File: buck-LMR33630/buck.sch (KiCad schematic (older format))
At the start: 22 parts, among them J1 USB-C Connector, P1 BATT-P, P2 BATT-N, P3 5V, SW1 RST, U1 LMR33630ADDA

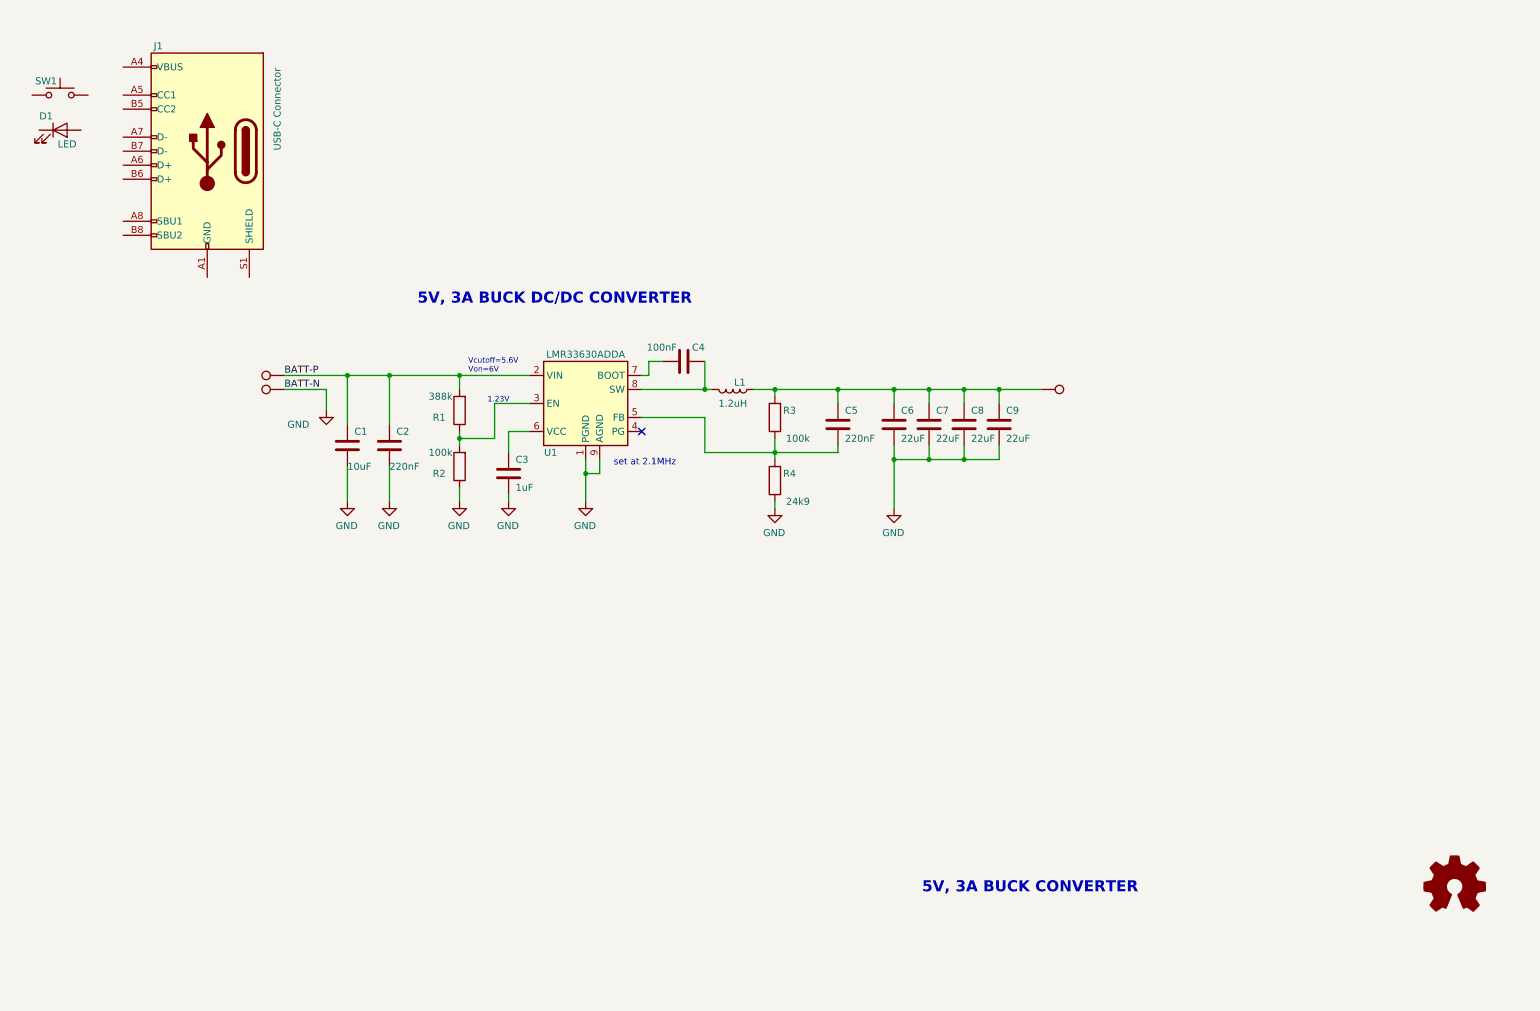
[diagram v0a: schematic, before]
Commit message: routed buck converter and added usb type c connector
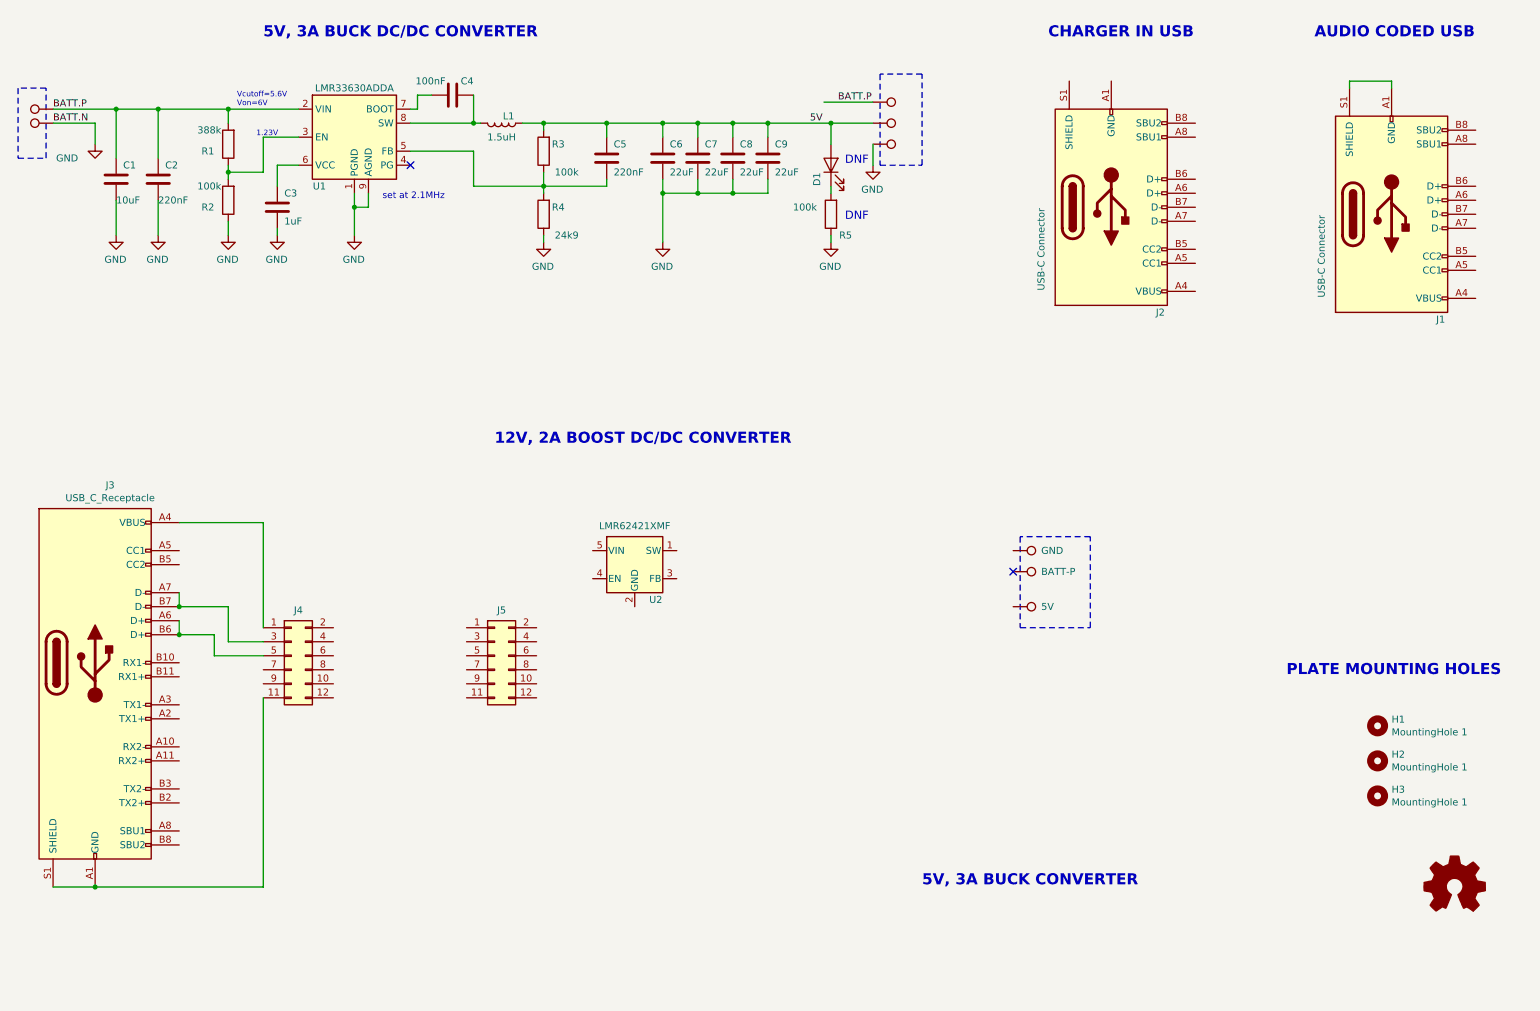
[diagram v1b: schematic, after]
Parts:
- removed SW1: RST, Button_Switch_SMD:SW_SPST_FSMSM, symbol Switch:SW_Push
- added H1, H2, H3: MountingHole 1, MountingHole:MountingHole_3.2mm_M3_Pad_Via, symbol Mechanical:MountingHole
- added J2: USB-C Connector, Connector_USB:USB_C_Receptacle_GCT_USB4085, symbol Connector:USB_C_Receptacle_USB2.0
- added J3: USB_C_Receptacle, Connector_USB:USB_C_Plug_JAE_DX07P024AJ1, symbol Connector:USB_C_Receptacle
- added J4, J5: Conn_02x06_Odd_Even, Connector_PinHeader_2.00mm:PinHeader_2x06_P2.00mm_Vertical, symbol Connector_Generic:Conn_02x06_Odd_Even
- added P4: 5V, TestPoint:TestPoint_Pad_4.0x4.0mm, symbol Connector:TestPoint
- added P5: Pad BATT.P, TestPoint:TestPoint_Pad_4.0x4.0mm, symbol Connector:TestPoint
- added P6: Pad 5V, TestPoint:TestPoint_Pad_4.0x4.0mm, symbol Connector:TestPoint
- added P7: Pad GND, TestPoint:TestPoint_Pad_4.0x4.0mm, symbol Connector:TestPoint
- added P8: BATT-P, TestPoint:TestPoint_Pad_4.0x4.0mm, symbol Connector:TestPoint
- added R5: 100k, Resistor_SMD:R_0805_2012Metric_Pad1.15x1.40mm_HandSolder, symbol Device:R
- added U2: LMR62421XMF, Package_TO_SOT_SMD:SOT-23-5, symbol Regulator_Switching:LMR62421XMF
- C1: Description CAP CER 10uF 100V X7S 0805 -> CAP CER 10uF 25V X5S 0805; MPN none -> TMK212BBJ106MGHT; Mouser PN none -> 963-TMK212BBJ106MGHT; Mouser Price none -> $0.22
- C6, C7, C8, C9: footprint Capacitor_SMD:C_0805_2012Metric_Pad1.15x1.40mm_HandSolder -> Capacitor_SMD:C_1206_3216Metric; Description CAP CER 22uF 50V X7S 0805 -> CAP CER 22uF 25V X5S 1206; MPN none -> TMK316BBJ226ML-T; Mouser PN none -> 963-TMK316BBJ226ML-T; Mouser Price none -> $0.55
- D1: Digikey Price $0.18 -> none
- J1: Digikey Price $1.1 -> none
- L1: value 1.2uH -> 1.5uH; footprint Inductor_SMD:L_Coilcraft_XxL4020 -> Inductor_SMD:L_Wuerth_MAPI-3020; Description Fixed Inductor 1.2uH 20% 9A 19.5mOhms AEC-Q200 -> Fixed Inductor 1.5uH 20% 3.8A 3020; MPN XEL4020-122MEC -> SRP3020TA-1R5M; Manufacturer Coilcraft -> Bourns; Mouser PN 994-XEL4020-122MEC -> 652-SRP3020TA-1R5M; Mouser Price $1.90 -> $0.85
- P3: value 5V -> GND; footprint TestPoint:TestPoint_THTPad_D1.5mm_Drill0.7mm -> TestPoint:TestPoint_Pad_4.0x4.0mm
- R1, R2, R3, R4: Digikey Price $0.10 -> none
- logo1: footprint Symbol:OSHW-Logo2_9.8x8mm_SilkScreen -> Symbol:OSHW-Symbol_6.7x6mm_SilkScreen
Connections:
- net GND: now also P7.1, R5.1
- net 5V: now reaches C5.1, C6.1, C7.1, C8.1, C9.1, L1.1, R3.2
- net 5V: now also D1.2 (A), P6.1; no longer P3.1
- net at J1.A1 (GND), J1.A12 (GND), J1.B1 (GND)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: now also J1.S1 (SHIELD)
- net at D1.1 (K): now also R5.2
- net BATT-P renamed BATT.P
- net BATT.P: now also P5.1
- new net: J2.A1 (GND), J2.A12 (GND), J2.B1 (GND), J2.B12 (GND)
- new net: J2.A4 (VBUS), J2.A9 (VBUS), J2.B4 (VBUS), J2.B9 (VBUS)
- new net: J3.A1 (GND), J3.A12 (GND), J3.B1 (GND), J3.B12 (GND), J3.S1 (SHIELD), J4.11 (Pin_11)
- new net: J3.A4 (VBUS), J3.A9 (VBUS), J3.B4 (VBUS), J3.B9 (VBUS), J4.1 (Pin_1)
- new net: J3.A6 (D+), J3.B6 (D+), J4.5 (Pin_5)
- new net: J3.A7 (D-), J3.B7 (D-), J4.3 (Pin_3)
- no-connect marks 1 -> 2
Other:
- note added: "12V, 2A BOOST DC/DC CONVERTER"
- note added: "AUDIO CODED USB"
- note added: "CHARGER IN USB"
- note added: "DNF"
- note added: "PLATE MOUNTING HOLES"
- moved on the sheet: C1, C2, C3, C4, C5, C6, C7, C8, C9, D1, J1, L1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

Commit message: added lithium c2S charger and tried to route USB3... quite difficult
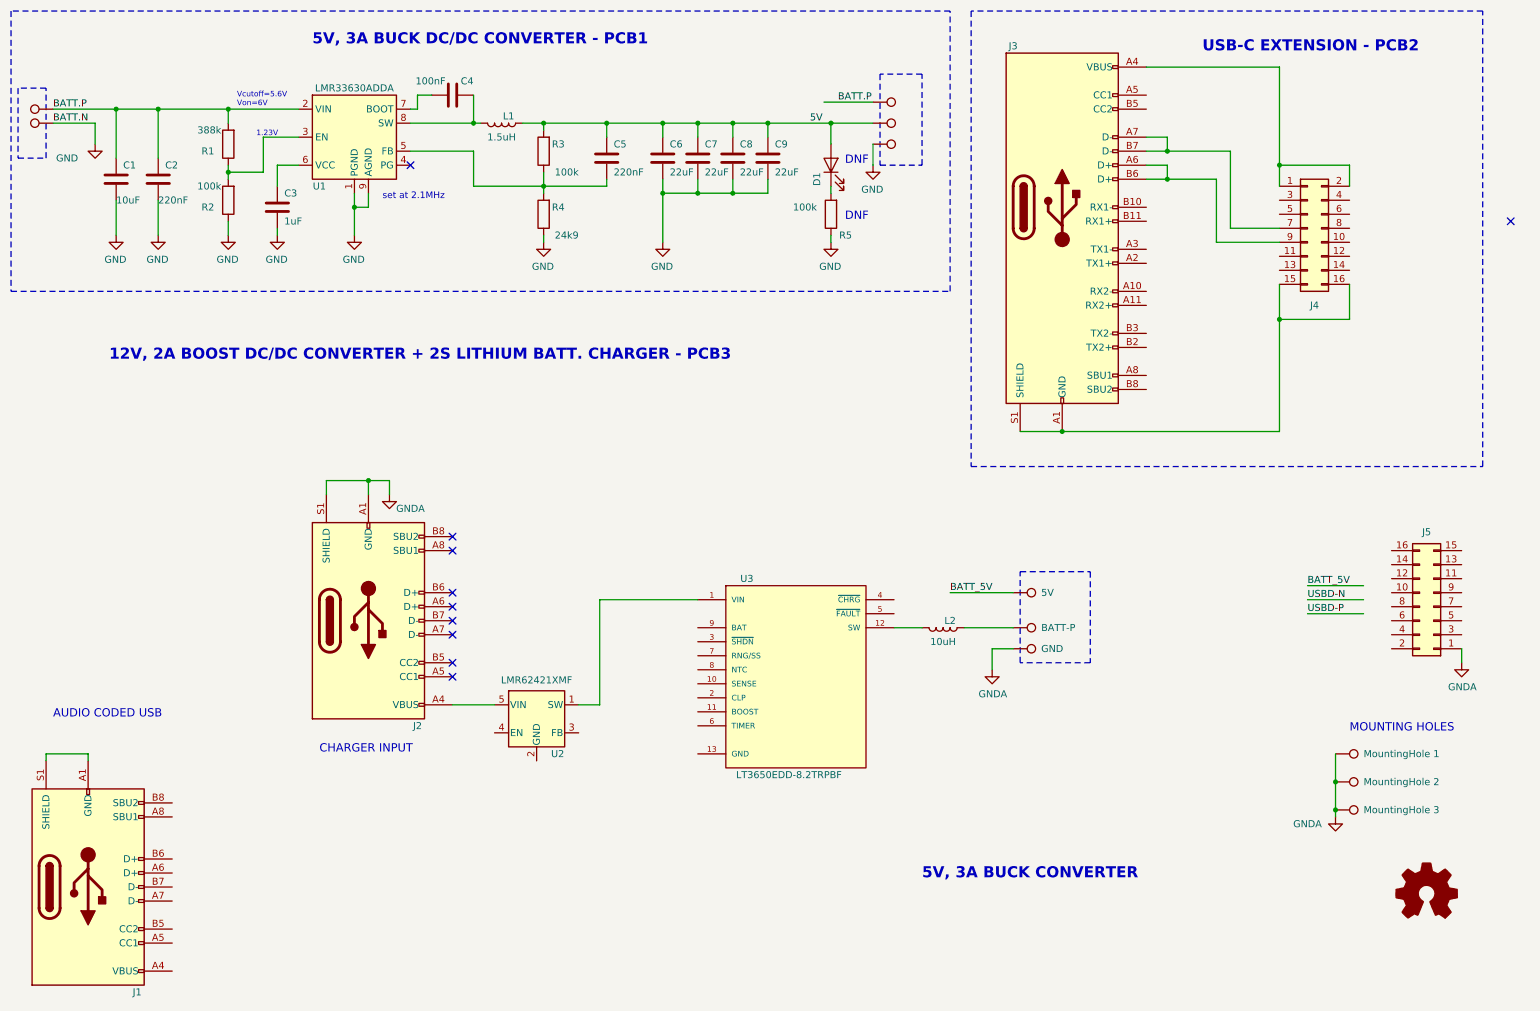
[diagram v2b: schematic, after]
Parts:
- removed H1, H2, H3: MountingHole 1, MountingHole:MountingHole_3.2mm_M3_Pad_Via, symbol Mechanical:MountingHole
- removed J4, J5: Conn_02x06_Odd_Even, Connector_PinHeader_2.00mm:PinHeader_2x06_P2.00mm_Vertical, symbol Connector_Generic:Conn_02x06_Odd_Even
- added H1: MountingHole 1, MountingHole:MountingHole_3.2mm_M3_Pad_Via, symbol Connector:TestPoint
- added H2: MountingHole 2, MountingHole:MountingHole_3.2mm_M3_Pad_Via, symbol Connector:TestPoint
- added H3: MountingHole 3, MountingHole:MountingHole_3.2mm_M3_Pad_Via, symbol Connector:TestPoint
- added J4, J5: Conn_02x08_Odd_Even, Connector_PinHeader_2.00mm:PinHeader_2x08_P2.00mm_Vertical, symbol Connector_Generic:Conn_02x08_Odd_Even
- added L2: 10uH, Inductor_SMD:L_Wuerth_MAPI-4030, symbol Device:L
- added U3: LT3650EDD-8.2TRPBF, Package_SO:MSOP-12-1EP_3x4mm_P0.65mm_EP1.65x2.85mm_ThermalVias, symbol LT3650EDD-8.2TRPBF:LT3650EDD-8.2TRPBF
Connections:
- net labels added: BATT_5V, GNDA, USBD-N, USBD-P
- wire segments 81 -> 112
- no-connect marks 2 -> 10
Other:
- note added: "12V, 2A BOOST DC/DC CONVERTER + 2S LITHIUM BATT. CHARGER - PCB3"
- note added: "5V, 3A BUCK DC/DC CONVERTER - PCB1"
- note added: "CHARGER INPUT"
- note added: "MOUNTING HOLES"
- note added: "USB-C EXTENSION - PCB2"
- note removed: "12V, 2A BOOST DC/DC CONVERTER"
- note removed: "5V, 3A BUCK DC/DC CONVERTER"
- note removed: "CHARGER IN USB"
- note removed: "PLATE MOUNTING HOLES"
- moved on the sheet: J1, J2, J3, U2
